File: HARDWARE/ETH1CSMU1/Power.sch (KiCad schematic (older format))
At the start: 150 parts, among them Q1301 IRFR5410, Q1302 Si7456DP, Q1303 SI7850DP, Q1304 FDMC5614P, Q1305 FDMC5614P, U1301 MAX5902, U1302 TEN 40-2415N, U1303 LT3758, U1304 LT3758, U1305 LTC3864, U1306 LTC3864, U1307 NCP1117-ADJ_TO252, U1308 LM337_TO252, U1309 NCP1117-3.3_TO252, U1310 NCP1117-3.3_TO252, U1311 NCP1117-5.0_TO252

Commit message: Footprints
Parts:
- C1302, C1305, C1306, C1307, C1308, C1309, C1310, C1313, C1314, C1315, C1316: footprint (none) -> SMD:C_1210_1
- C1303, C1304: footprint (none) -> Capacitors_SMD:C_1206
- C1317, C1318, C1319, C1339, C1340: footprint (none) -> Capacitors_SMD:C_0603
- C1321, C1322: footprint (none) -> SMD:C_0603_Symbol1
- C1323, C1324, C1327, C1328: footprint (none) -> SMD:C_0603_Symbol4
- C1325, C1326: footprint (none) -> SMD:C_0603_Symbol2
- C1329, C1330: value 4u7/50V/X5R -> 4u7/50V/X7R; footprint (none) -> SMD:C_1210_1
- C1333, C1334, C1335, C1336: footprint (none) -> Capacitors_SMD:C_1206_HandSoldering
- D1301: value TVS_UPOL -> SM6T30AY; footprint (none) -> SMD:DO_214AA_REV
- F1301: value Fuse -> MF-LSMF185/33X; footprint (none) -> SMD:Fuse_SMD2920
- FB1301, FB1302, FB1303, FB1304, FB1305: footprint (none) -> SMD:R_0805_Symbol1
- Q1301: footprint (none) -> TO_SOT_Packages_SMD:TO-252-2_Rectifier
- R1301, R1316, R1317, R1332, R1333: footprint (none) -> SMD:R_0603_Symbol3
- R1318, R1319: footprint (none) -> SMD:R_0603_Symbol1
- U1301: footprint (none) -> SMD:SOT23_6
- U1307, U1308, U1309, U1310, U1311: footprint Package_TO_SOT_SMD:TO-252-2 -> SMD:DPAK

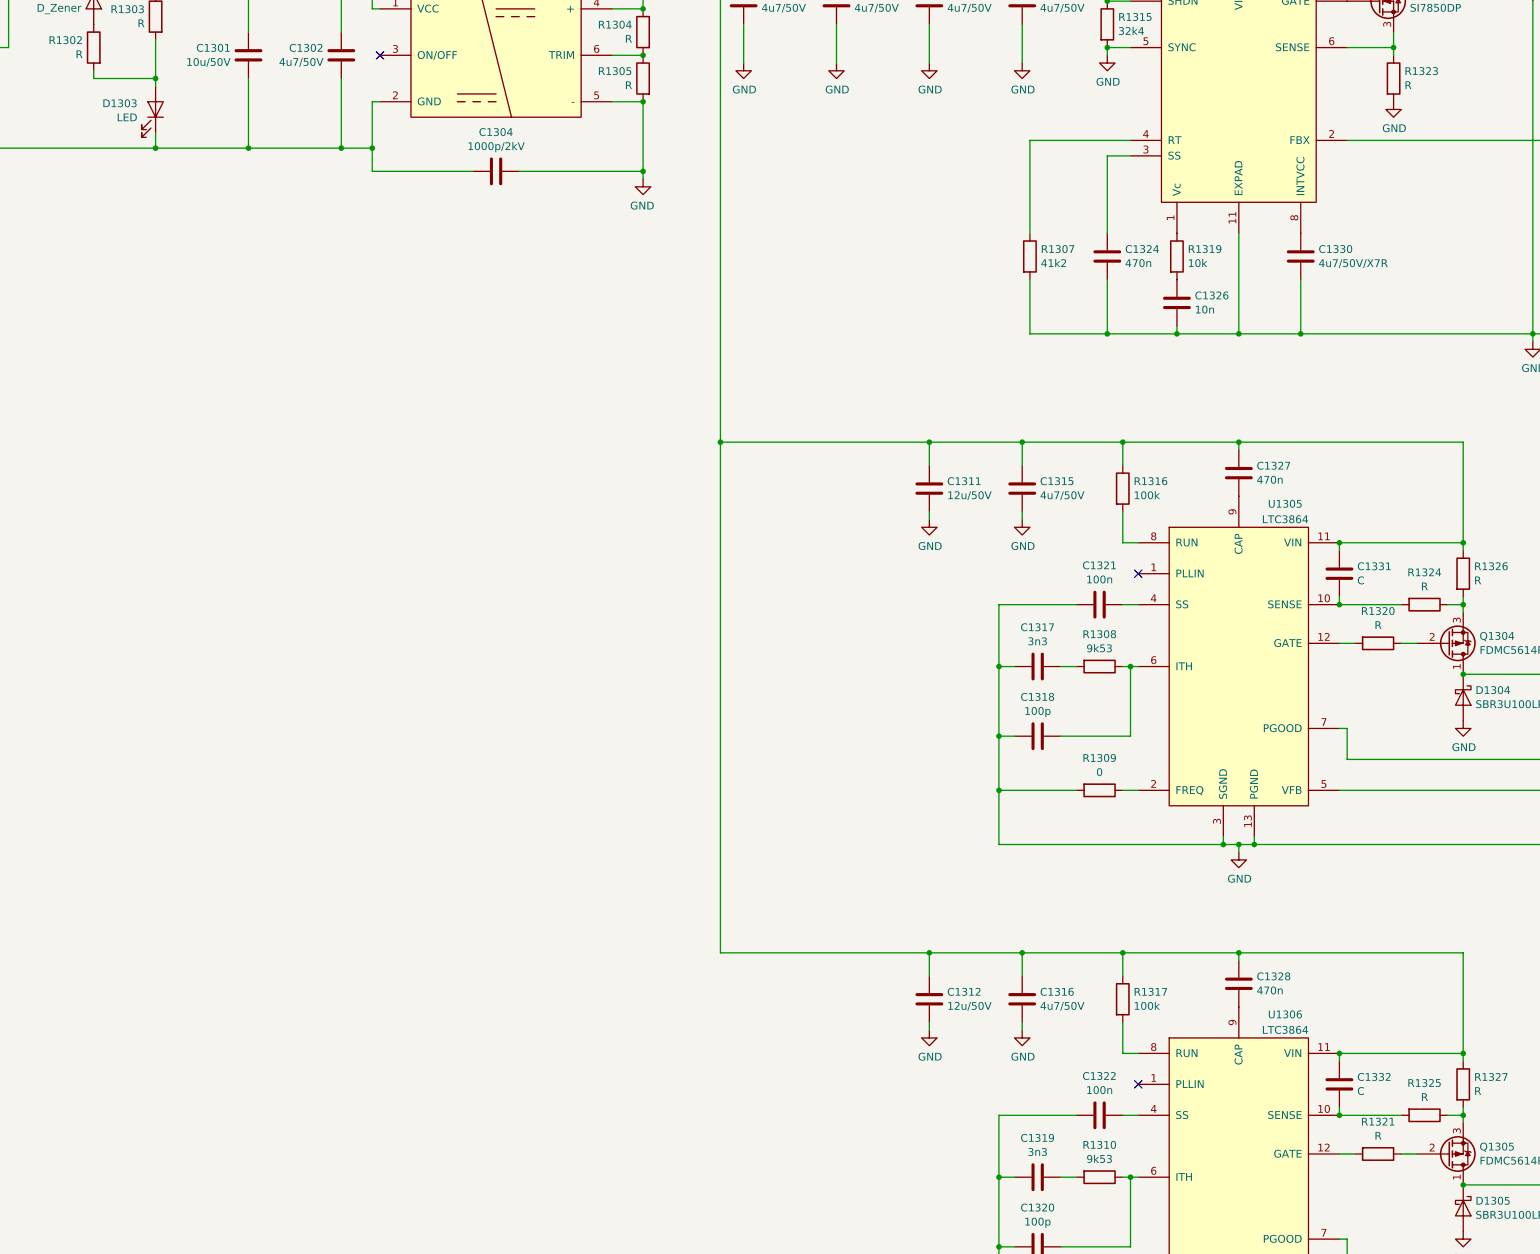
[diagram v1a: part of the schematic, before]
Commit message: Footprint selection
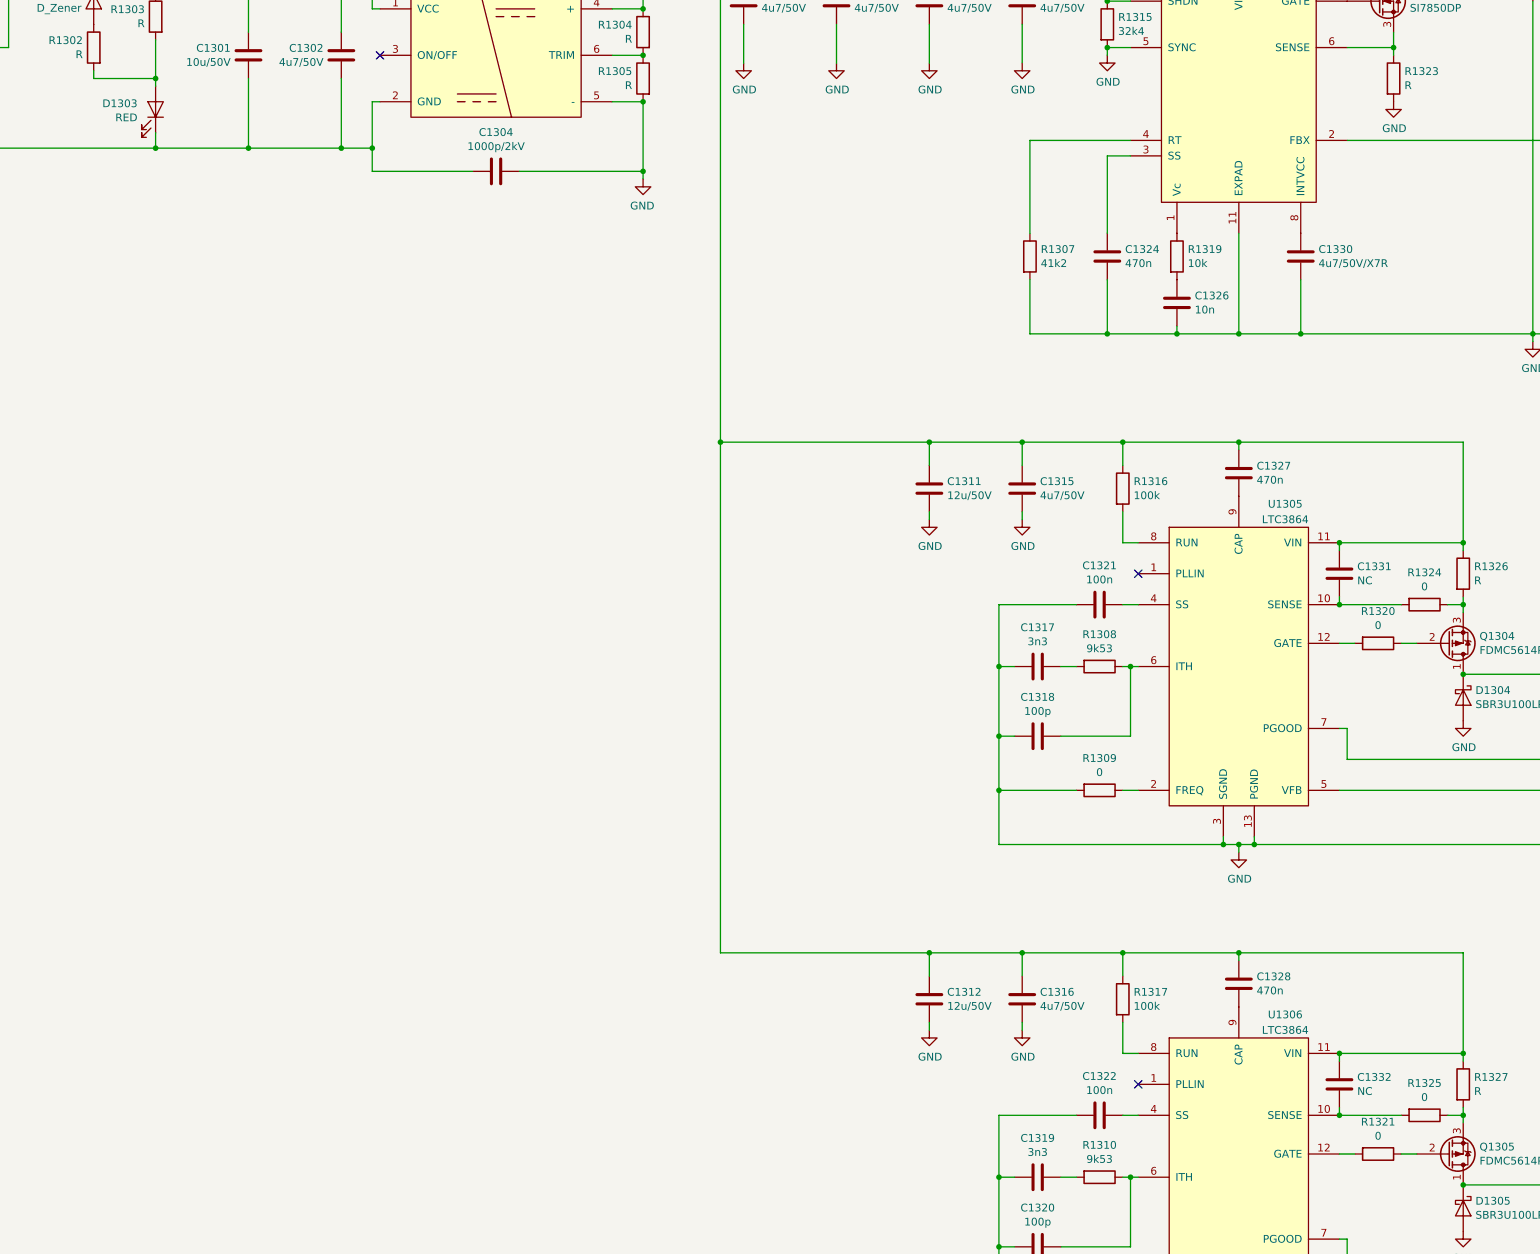
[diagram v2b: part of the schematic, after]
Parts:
- C1320: footprint (none) -> Capacitors_SMD:C_0603
- C1331, C1332: value C -> NC; footprint (none) -> Capacitors_SMD:C_0603
- D1303: value LED -> RED; footprint (none) -> LEDs:LED_0603
- R1306, R1307, R1308, R1310, R1312, R1313, R1314, R1315, R1334, R1335, R1343: footprint (none) -> Resistors_SMD:R_0603
- R1309, R1311: footprint (none) -> SMD:R_0603_Symbol2
- R1320, R1321, R1324, R1325: value R -> 0; footprint (none) -> SMD:R_0603_Symbol2
- U1302: footprint (none) -> THT:TEN40
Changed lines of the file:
@@
 P 5150 6350
 F 0 "D1303" V 5188 6233 50  0000 R CNN
-F 1 "LED" V 5097 6233 50  0000 R CNN
-F 2 "" H 5150 6350 50  0001 C CNN
+F 1 "RED" V 5097 6233 50  0000 R CNN
+F 2 "LEDs:LED_0603" H 5150 6350 50  0001 C CNN
 F 3 "~" H 5150 6350 50  0001 C CNN
 	1    5150 6350
@@
 F 0 "U1302" H 7350 6565 50  0000 C CNN
 F 1 "TEN 40-2415N" H 7350 6474 50  0000 C CNN
-F 2 "" H 7350 6000 50  0001 C CNN
+F 2 "THT:TEN40" H 7350 6000 50  0001 C CNN
 F 3 "" H 7350 6000 50  0001 C CNN
 	1    7350 6000
@@
 F 0 "R1313" H 11370 2096 50  0000 L CNN
 F 1 "32k4" H 11370 2005 50  0000 L CNN
-F 2 "" V 11230 2050 50  0001 C CNN
+F 2 "Resistors_SMD:R_0603" V 11230 2050 50  0001 C CNN
 F 3 "~" H 11300 2050 50  0001 C CNN
 	1    11300 2050
@@
 F 0 "R1312" H 11370 1746 50  0000 L CNN
 F 1 "154k" H 11370 1655 50  0000 L CNN
-F 2 "" V 11230 1700 50  0001 C CNN
+F 2 "Resistors_SMD:R_0603" V 11230 1700 50  0001 C CNN
 F 3 "~" H 11300 1700 50  0001 C CNN
 	1    11300 1700
@@
 F 0 "R1306" H 10870 3596 50  0000 L CNN
 F 1 "41k2" H 10870 3505 50  0000 L CNN
-F 2 "" V 10730 3550 50  0001 C CNN
+F 2 "Resistors_SMD:R_0603" V 10730 3550 50  0001 C CNN
 F 3 "~" H 10800 3550 50  0001 C CNN
 	1    10800 3550
@@
 F 0 "R1315" H 11370 5846 50  0000 L CNN
 F 1 "32k4" H 11370 5755 50  0000 L CNN
-F 2 "" V 11230 5800 50  0001 C CNN
+F 2 "Resistors_SMD:R_0603" V 11230 5800 50  0001 C CNN
 F 3 "~" H 11300 5800 50  0001 C CNN
 	1    11300 5800
@@
 F 0 "R1314" H 11370 5496 50  0000 L CNN
 F 1 "200k" H 11370 5405 50  0000 L CNN
-F 2 "" V 11230 5450 50  0001 C CNN
+F 2 "Resistors_SMD:R_0603" V 11230 5450 50  0001 C CNN
 F 3 "~" H 11300 5450 50  0001 C CNN
 	1    11300 5450
@@
 F 0 "R1307" H 10870 7346 50  0000 L CNN
 F 1 "41k2" H 10870 7255 50  0000 L CNN
-F 2 "" V 10730 7300 50  0001 C CNN
+F 2 "Resistors_SMD:R_0603" V 10730 7300 50  0001 C CNN
 F 3 "~" H 10800 7300 50  0001 C CNN
 	1    10800 7300
@@
 F 0 "R1308" V 11043 9950 50  0000 C CNN
 F 1 "9k53" V 11134 9950 50  0000 C CNN
-F 2 "" V 11180 9950 50  0001 C CNN
+F 2 "Resistors_SMD:R_0603" V 11180 9950 50  0001 C CNN
 F 3 "~" H 11250 9950 50  0001 C CNN
 	1    11250 9950
@@
 F 0 "R1309" V 11043 10750 50  0000 C CNN
 F 1 "0" V 11134 10750 50  0000 C CNN
-F 2 "" V 11180 10750 50  0001 C CNN
+F 2 "SMD:R_0603_Symbol2" V 11180 10750 50  0001 C CNN
 F 3 "~" H 11250 10750 50  0001 C CNN
 	1    11250 10750
@@
 F 0 "R1334" H 15820 10646 50  0000 L CNN
 F 1 "422k" H 15820 10555 50  0000 L CNN
-F 2 "" V 15680 10600 50  0001 C CNN
+F 2 "Resistors_SMD:R_0603" V 15680 10600 50  0001 C CNN
 F 3 "~" H 15750 10600 50  0001 C CNN
 	1    15750 10600
@@
 F 0 "R1335" H 15820 10946 50  0000 L CNN
 F 1 "80k6" H 15820 10855 50  0000 L CNN
-F 2 "" V 15680 10900 50  0001 C CNN
+F 2 "Resistors_SMD:R_0603" V 15680 10900 50  0001 C CNN
 F 3 "~" H 15750 10900 50  0001 C CNN
 	1    15750 10900
@@
 P 12800 9350
 F 0 "C1331" H 12915 9396 50  0000 L CNN
-F 1 "C" H 12915 9305 50  0000 L CNN
-F 2 "" H 12838 9200 50  0001 C CNN
+F 1 "NC" H 12915 9305 50  0000 L CNN
+F 2 "Capacitors_SMD:C_0603" H 12838 9200 50  0001 C CNN
 F 3 "~" H 12800 9350 50  0001 C CNN
 	1    12800 9350
@@
 P 13350 9550
 F 0 "R1324" V 13143 9550 50  0000 C CNN
-F 1 "R" V 13234 9550 50  0000 C CNN
-F 2 "" V 13280 9550 50  0001 C CNN
+F 1 "0" V 13234 9550 50  0000 C CNN
+F 2 "SMD:R_0603_Symbol2" V 13280 9550 50  0001 C CNN
 F 3 "~" H 13350 9550 50  0001 C CNN
 	1    13350 9550
@@
 P 13050 9800
 F 0 "R1320" V 12843 9800 50  0000 C CNN
-F 1 "R" V 12934 9800 50  0000 C CNN
-F 2 "" V 12980 9800 50  0001 C CNN
+F 1 "0" V 12934 9800 50  0000 C CNN
+F 2 "SMD:R_0603_Symbol2" V 12980 9800 50  0001 C CNN
 F 3 "~" H 13050 9800 50  0001 C CNN
 	1    13050 9800
@@
 F 0 "R1310" V 11043 13250 50  0000 C CNN
 F 1 "9k53" V 11134 13250 50  0000 C CNN
-F 2 "" V 11180 13250 50  0001 C CNN
+F 2 "Resistors_SMD:R_0603" V 11180 13250 50  0001 C CNN
 F 3 "~" H 11250 13250 50  0001 C CNN
 	1    11250 13250
@@
 F 0 "C1320" V 10598 13700 50  0000 C CNN
 F 1 "100p" V 10689 13700 50  0000 C CNN
-F 2 "" H 10888 13550 50  0001 C CNN
+F 2 "Capacitors_SMD:C_0603" H 10888 13550 50  0001 C CNN
 F 3 "~" H 10850 13700 50  0001 C CNN
 	1    10850 13700
@@
 F 0 "R1311" V 11043 14050 50  0000 C CNN
 F 1 "0" V 11134 14050 50  0000 C CNN
-F 2 "" V 11180 14050 50  0001 C CNN
+F 2 "SMD:R_0603_Symbol2" V 11180 14050 50  0001 C CNN
 F 3 "~" H 11250 14050 50  0001 C CNN
 	1    11250 14050
@@
 P 12800 12650
 F 0 "C1332" H 12915 12696 50  0000 L CNN
-F 1 "C" H 12915 12605 50  0000 L CNN
-F 2 "" H 12838 12500 50  0001 C CNN
+F 1 "NC" H 12915 12605 50  0000 L CNN
+F 2 "Capacitors_SMD:C_0603" H 12838 12500 50  0001 C CNN
 F 3 "~" H 12800 12650 50  0001 C CNN
 	1    12800 12650
@@
 P 13350 12850
 F 0 "R1325" V 13143 12850 50  0000 C CNN
-F 1 "R" V 13234 12850 50  0000 C CNN
-F 2 "" V 13280 12850 50  0001 C CNN
+F 1 "0" V 13234 12850 50  0000 C CNN
+F 2 "SMD:R_0603_Symbol2" V 13280 12850 50  0001 C CNN
 F 3 "~" H 13350 12850 50  0001 C CNN
 	1    13350 12850
@@
 P 13050 13100
 F 0 "R1321" V 12843 13100 50  0000 C CNN
-F 1 "R" V 12934 13100 50  0000 C CNN
-F 2 "" V 12980 13100 50  0001 C CNN
+F 1 "0" V 12934 13100 50  0000 C CNN
+F 2 "SMD:R_0603_Symbol2" V 12980 13100 50  0001 C CNN
 F 3 "~" H 13050 13100 50  0001 C CNN
 	1    13050 13100
@@
 F 0 "R1343" H 18820 5496 50  0000 L CNN
 F 1 "120" H 18820 5405 50  0000 L CNN
-F 2 "" V 18680 5450 50  0001 C CNN
+F 2 "Resistors_SMD:R_0603" V 18680 5450 50  0001 C CNN
 F 3 "~" H 18750 5450 50  0001 C CNN
 	1    18750 5450

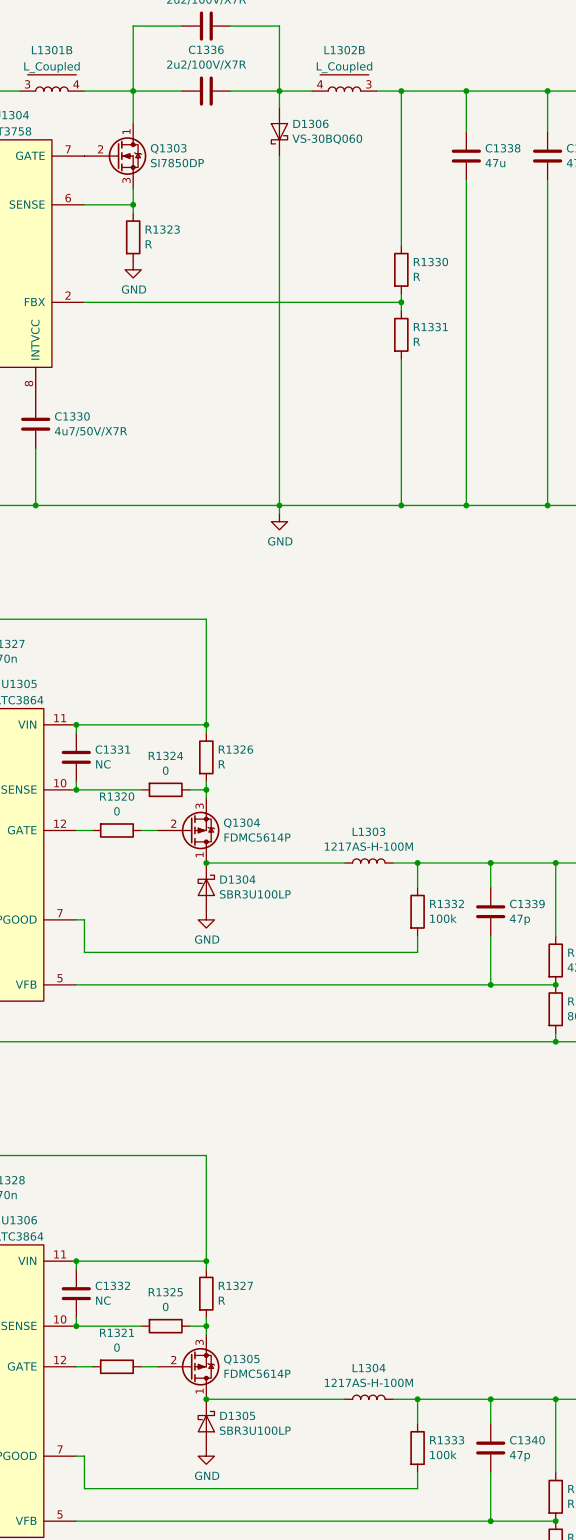
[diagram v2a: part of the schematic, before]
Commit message: Redesigned feedback circuit.
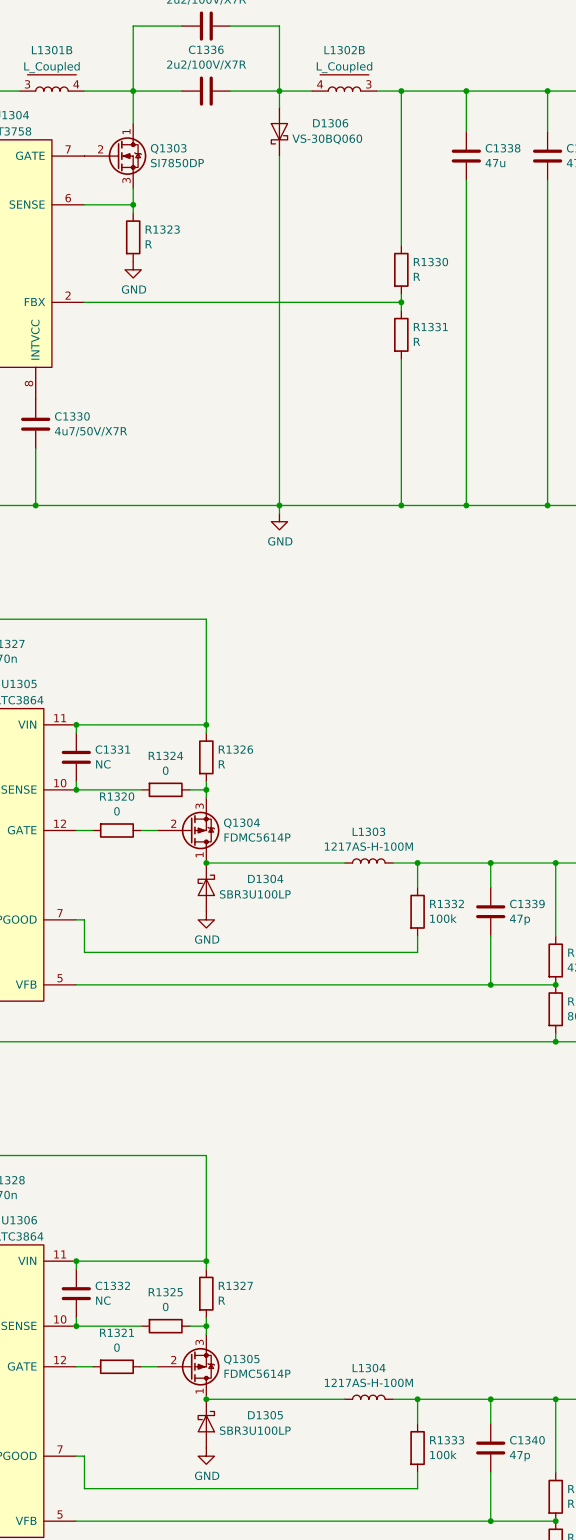
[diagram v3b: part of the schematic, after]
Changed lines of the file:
@@
 U 1 1 5C08C6DE
 P 14050 5500
-F 0 "D1306" V 14096 5421 50  0000 R CNN
+F 0 "D1306" V 14100 5300 50  0000 R CNN
 F 1 "VS-30BQ060" V 14005 5421 50  0000 R CNN
 F 2 "" H 14050 5500 50  0001 C CNN
@@
 U 1 1 5C3A7E35
 P 13600 10150
-F 0 "D1304" V 13554 10229 50  0000 L CNN
+F 0 "D1304" V 13550 10400 50  0000 L CNN
 F 1 " SBR3U100LP" V 13645 10229 50  0000 L CNN
 F 2 "" H 13600 10150 50  0001 C CNN
@@
 U 1 1 5CB39397
 P 13600 13450
-F 0 "D1305" V 13554 13529 50  0000 L CNN
+F 0 "D1305" V 13550 13700 50  0000 L CNN
 F 1 " SBR3U100LP" V 13645 13529 50  0000 L CNN
 F 2 "" H 13600 13450 50  0001 C CNN

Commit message: Schematic development
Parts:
- renumbered C1301 to C1201, C1302 to C1202, C1303 to C1203, C1304 to C1204, C1305 to C1205, C1306 to C1206, C1307 to C1207, C1308 to C1208, C1309 to C1209, C1310 to C1210, C1311 to C1211, C1312 to C1212, C1313 to C1213, C1314 to C1214, C1315 to C1215, C1316 to C1216, C1317 to C1217, C1318 to C1218, C1319 to C1219, C1320 to C1220, C1321 to C1221, C1322 to C1222, C1323 to C1223, C1324 to C1224, C1325 to C1225, C1326 to C1226, C1327 to C1227, C1328 to C1228, C1329 to C1229, C1330 to C1230, C1331 to C1231, C1332 to C1232, C1333 to C1233, C1334 to C1234, C1335 to C1235, C1336 to C1236, C1337 to C1237, C1338 to C1238, C1339 to C1239, C1340 to C1240, C1341 to C1241, C1342 to C1242, C1343 to C1243, C1344 to C1244, C1345 to C1245, C1346 to C1246, C1347 to C1247, C1348 to C1248, C1349 to C1249, C1350 to C1250, C1351 to C1251, C1352 to C1252, C1353 to C1253, C1354 to C1254, C1355 to C1255, C1356 to C1256, C1357 to C1257, C1358 to C1258, C1359 to C1259, C1360 to C1260, C1361 to C1261, C1362 to C1262, C1363 to C1263, C1364 to C1264, C1365 to C1265, C1366 to C1266, C1367 to C1267, C1368 to C1268, C1369 to C1269, C1370 to C1270, C1371 to C1271, C1372 to C1272, C1373 to C1273, C1374 to C1274, D1301 to D1201, D1302 to D1202, D1303 to D1203, D1304 to D1204, D1305 to D1205, D1306 to D1206, D1307 to D1207, F1301 to F1201, FB1301 to FB1201, FB1302 to FB1202, FB1303 to FB1203, FB1304 to FB1204, FB1305 to FB1205, L1301 to L1201, L1302 to L1202, L1303 to L1203, L1304 to L1204, Q1301 to Q1201, Q1302 to Q1202, Q1303 to Q1203, Q1304 to Q1204, Q1305 to Q1205, R1301 to R1201, R1302 to R1202, R1303 to R1203, R1304 to R1204, R1305 to R1205, R1306 to R1206, R1307 to R1207, R1308 to R1208, R1309 to R1209, R1310 to R1210, R1311 to R1211, R1312 to R1212, R1313 to R1213, R1314 to R1214, R1315 to R1215, R1316 to R1216, R1317 to R1217, R1318 to R1218, R1319 to R1219, R1320 to R1220, R1321 to R1221, R1322 to R1222, R1323 to R1223, R1324 to R1224, R1325 to R1225, R1326 to R1226, R1327 to R1227, R1328 to R1228, R1329 to R1229, R1330 to R1230, R1331 to R1231, R1332 to R1232, R1333 to R1233, R1334 to R1234, R1335 to R1235, R1336 to R1236, R1337 to R1237, R1338 to R1238, R1339 to R1239, R1340 to R1240, R1341 to R1241, R1342 to R1242, R1343 to R1243, U1301 to U1201, U1302 to U1202, U1303 to U1203, U1304 to U1204, U1305 to U1205, U1306 to U1206, U1307 to U1207, U1308 to U1208, U1309 to U1209, U1310 to U1210, U1311 to U1211
